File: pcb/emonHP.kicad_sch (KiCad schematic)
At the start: 23 parts, among them J1 USB_C_Receptacle_USB2.0, J2 Screw_Terminal_01x03, J3 Screw_Terminal_01x03, J4 Screw_Terminal_01x03, J5 Screw_Terminal_01x03, J6 Screw_Terminal_01x03, J7 Conn_ARM_JTAG_SWD_10, J8 Raspberry_Pi_2_3, U1 ATSAMD21G17A-A, U2 USBLC6-2P6, U3 AP2112K-3.3, U4 THVD1400D

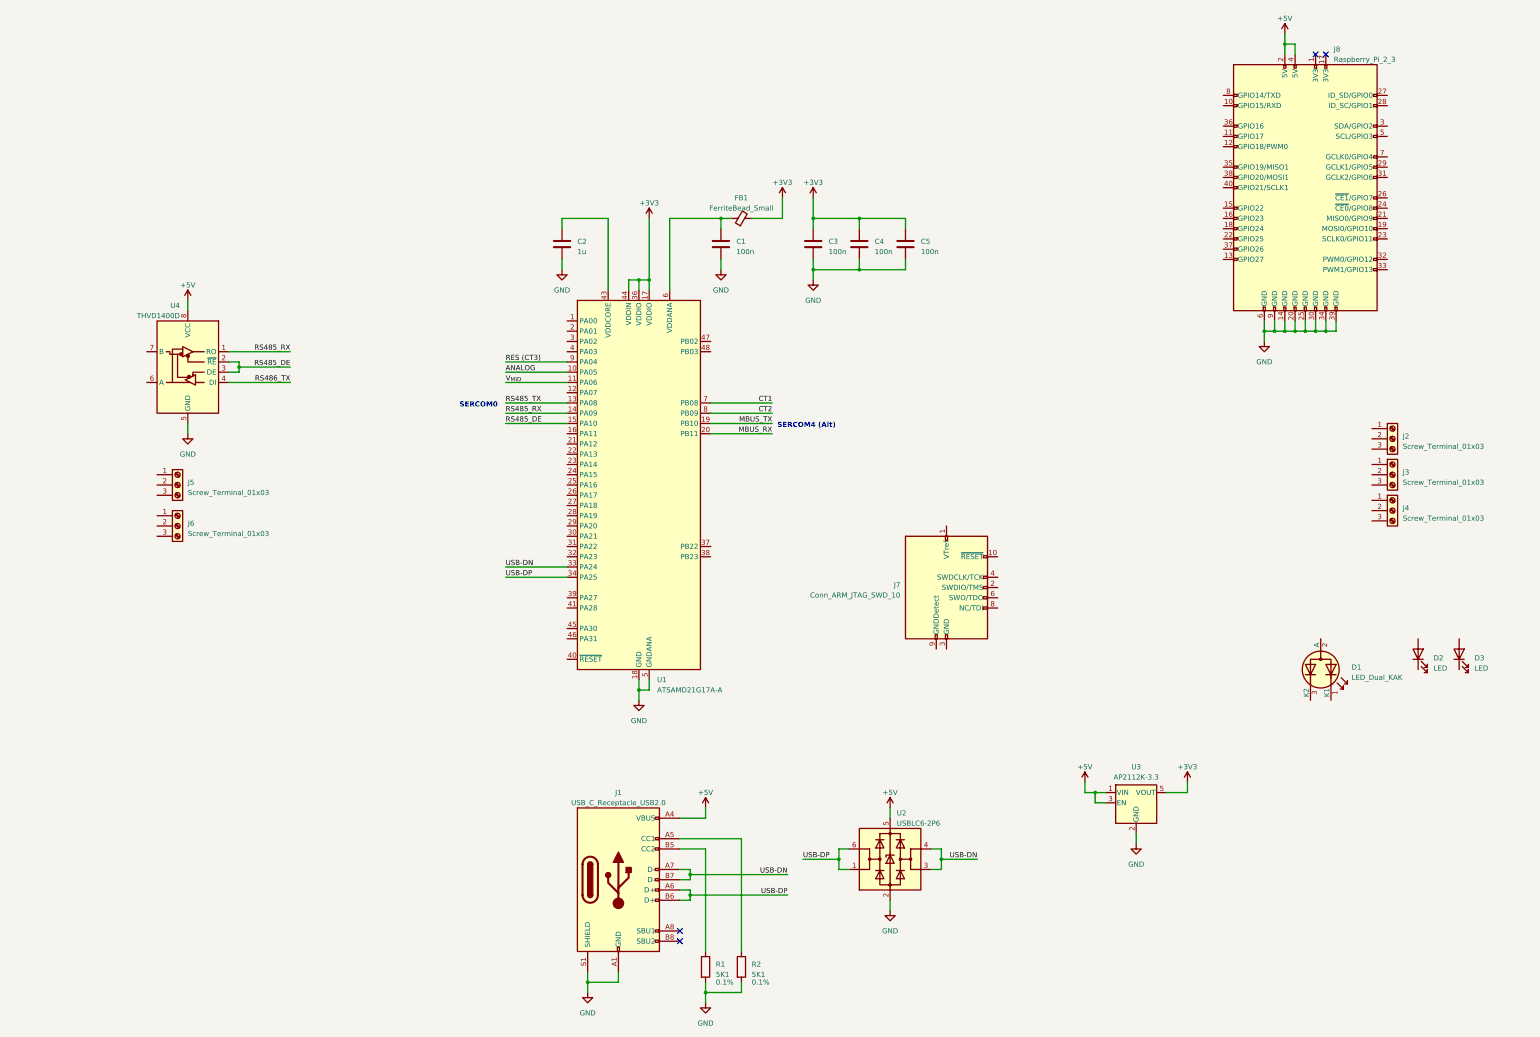
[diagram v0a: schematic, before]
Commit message: * Continue initial placement
  - External connectors added
  - Switch and indicator LED added
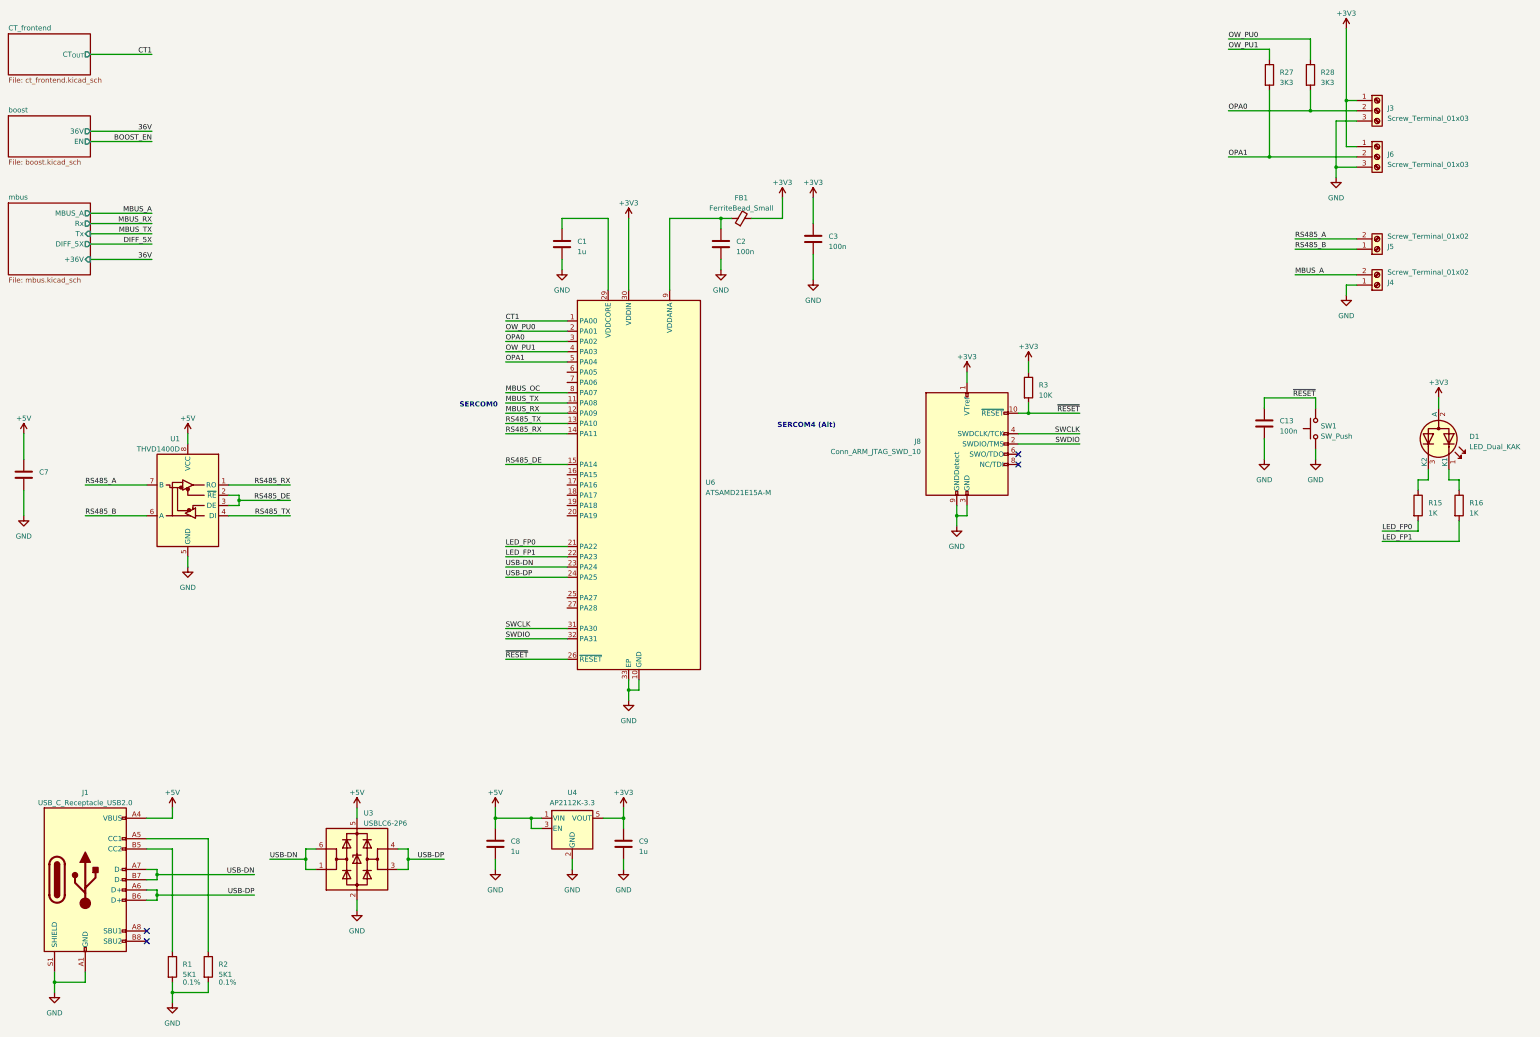
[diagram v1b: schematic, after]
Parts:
- removed C4, C5: 100n, Capacitor_SMD:C_0603_1608Metric, symbol Device:C
- removed D2, D3: LED, LED_SMD:LED_0805_2012Metric, symbol Device:LED
- removed J3, J4, J5: Screw_Terminal_01x03, TerminalBlock_Phoenix:TerminalBlock_Phoenix_PT-1,5-3-3.5-H_1x03_P3.50mm_Horizontal, symbol Connector:Screw_Terminal_01x03
- removed J7: Conn_ARM_JTAG_SWD_10, Connector_PinHeader_1.27mm:PinHeader_2x05_P1.27mm_Vertical_SMD, symbol Connector:Conn_ARM_JTAG_SWD_10
- removed J8: Raspberry_Pi_2_3, Connector_PinSocket_2.54mm:PinSocket_2x20_P2.54mm_Vertical_SMD, symbol Connector:Raspberry_Pi_2_3
- removed U1: ATSAMD21G17A-A, Package_QFP:TQFP-48_7x7mm_P0.5mm, symbol MCU_Microchip_SAMD:ATSAMD21G17A-A
- added C13, C7: 100n, Capacitor_SMD:C_0402_1005Metric, symbol Device:C
- added C8, C9: 1u, Capacitor_SMD:C_0402_1005Metric, symbol Device:C
- added J4, J5: Screw_Terminal_01x02, TerminalBlock_Phoenix:TerminalBlock_Phoenix_PT-1,5-2-3.5-H_1x02_P3.50mm_Horizontal, symbol Connector:Screw_Terminal_01x02
- added J8: Conn_ARM_JTAG_SWD_10, Connector_PinHeader_1.27mm:PinHeader_2x05_P1.27mm_Vertical_SMD, symbol Connector:Conn_ARM_JTAG_SWD_10
- added R15, R16: 1K, Resistor_SMD:R_0402_1005Metric, symbol Device:R
- added R27, R28: 3K3, Resistor_SMD:R_0402_1005Metric, symbol Device:R
- added R3: 10K, Resistor_SMD:R_0402_1005Metric, symbol Device:R
- added SW1: SW_Push, Button_Switch_SMD:Panasonic_EVQPUM_EVQPUD, symbol Switch:SW_Push
- added U6: ATSAMD21E15A-M, Package_DFN_QFN:QFN-32-1EP_5x5mm_P0.5mm_EP3.6x3.6mm, symbol MCU_Microchip_SAMD:ATSAMD21E15A-M
- C1: renamed from C2; footprint Capacitor_SMD:C_0603_1608Metric -> Capacitor_SMD:C_0402_1005Metric
- C2: renamed from C1; footprint Capacitor_SMD:C_0603_1608Metric -> Capacitor_SMD:C_0402_1005Metric
- C3: footprint Capacitor_SMD:C_0603_1608Metric -> Capacitor_SMD:C_0402_1005Metric
- FB1: footprint Inductor_SMD:L_0603_1608Metric -> Inductor_SMD:L_0402_1005Metric
- J1: footprint (none) -> valcon-usb:CSP-USC16-TR
- R1, R2: footprint (none) -> Resistor_SMD:R_0402_1005Metric
- renumbered J2 to J3, U4 to U1, U2 to U3, U3 to U4
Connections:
- net RS486_TX is gone; now on net RS485_TX: U1.4 (DI)
- net +3V3: now also D1.2 (A), J3.1 (Pin_1), J6.1 (Pin_1), C9.1, J8.1 (VTref), R3.1, U6.30 (VDDIN)
- net +5V: now also C7.1, C8.1
- net CT1: now also U6.1 (PA00)
- net GND: now also J3.3 (Pin_3), J6.3 (Pin_3), C13.2, C7.2, C8.2, C9.2, J4.1 (Pin_1), J8.3 (GND), J8.5 (GND), J8.9 (GNDDetect), SW1.1, U6.10 (GND), U6.28 (GND), U6.33 (EP)
- net MBUS_RX: now also U6.12 (PA09)
- net MBUS_TX: now also U6.11 (PA08)
- net RS485_DE: now also U6.15 (PA14)
- net RS485_RX: now also U6.14 (PA11)
- net RS485_TX: now also U6.13 (PA10)
- net USB-DN: now also U3.1 (I/O1), U3.6 (I/O1), U6.23 (PA24); no longer U3.3 (I/O2), U3.4 (I/O2)
- net USB-DP: now also U3.3 (I/O2), U3.4 (I/O2), U6.24 (PA25); no longer U3.1 (I/O1), U3.6 (I/O1)
- net OPA1: now reaches J6.2 (Pin_2)
- net OPA1: now also R27.2, U6.5 (PA04)
- net at C1.1: now also U6.29 (VDDCORE)
- net at C2.1, FB1.1: now also U6.9 (VDDANA)
- net OPA0: now reaches J3.2 (Pin_2)
- net OPA0: now also R28.2, U6.3 (PA02)
- net at D1.1 (K1): now also R16.1
- net at D1.3 (K2): now also R15.1
- net RS485_B: now reaches U1.6 (A)
- net RS485_B: now also J5.1 (Pin_1)
- net RS485_A: now reaches U1.7 (B)
- net RS485_A: now also J5.2 (Pin_2)
- new net LED_FP0: R15.2, U6.21 (PA22)
- new net LED_FP1: R16.2, U6.22 (PA23)
- new net MBUS_A: J4.2 (Pin_2)
- new net MBUS_OC: U6.8 (PA07)
- new net OW_PU0: R28.1, U6.2 (PA01)
- new net OW_PU1: R27.1, U6.4 (PA03)
- new net SWCLK: J8.4 (SWDCLK/TCK), U6.31 (PA30)
- new net SWDIO: J8.2 (SWDIO/TMS), U6.32 (PA31)
- new net ~{RESET}: C13.1, J8.10 (~{RESET}), R3.2, SW1.2, U6.26 (~{RESET})
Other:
- added sheet CT_frontend (ct_frontend.kicad_sch)
- added sheet boost (boost.kicad_sch)
- added sheet mbus (mbus.kicad_sch)
- company: OpenEnergyMonitor / Tilt Ltd -> Tilt Ltd / OpenEnergyMonitor
- moved on the sheet: C3, D1, J1, J3, R1, R2, U1, U3, U4

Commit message: * Work in progress
  - Add generate script
  - Add switch model
  - Start routing
  - Tidy schematic
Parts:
- added D10: LED, LED_SMD:LED_0805_2012Metric, symbol Device:LED
- added D13 (x3): ESD5Z3.3T5G, Diode_SMD:D_SOD-523, symbol Diode:ESD5Zxx
- added D5: CDSOT23-SM712, Package_TO_SOT_SMD:SOT-23, symbol Power_Protection:NUP2105L
- added J2: Conn_01x03, Connector_PinHeader_2.54mm:PinHeader_1x03_P2.54mm_Vertical, symbol Connector_Generic:Conn_01x03
- added R29, R30: 10R, Resistor_SMD:R_0603_1608Metric, symbol Device:R
- added R33: 1K, Resistor_SMD:R_0402_1005Metric, symbol Device:R
- J8: now not fitted
- SW1: footprint Button_Switch_SMD:Panasonic_EVQPUM_EVQPUD -> Button_Switch_SMD:Panasonic_EVQPUJ_EVQPUA
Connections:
- net +3V3: now also R33.1
- net BOOST_EN: now also U6.16 (PA15)
- net CT1: now also U6.3 (PA02); no longer U6.1 (PA00)
- net GND: now also D10.1 (K), D13.2 (A), D13.2 (A), D13.2 (A), D5.3 (A), J2.3 (Pin_3)
- net OPA0: now also U6.5 (PA04), D13.1 (K); no longer U6.3 (PA02)
- net OPA1: now also U6.7 (PA06), D13.1 (K); no longer U6.5 (PA04)
- net OW_PU0: now also U6.4 (PA03); no longer U6.2 (PA01)
- net OW_PU1: now also U6.6 (PA05); no longer U6.4 (PA03)
- net RS485_A: now also D5.1 (K), R29.1; no longer U1.7 (B)
- net RS485_B: now also D5.2 (K), R30.1; no longer U1.6 (A)
- net ~{RESET}: now also D13.1 (K)
- net DBG_TX: now reaches U6.19 (PA18)
- net DBG_TX: now also J2.1 (Pin_1)
- net DBG_RX: now reaches U6.20 (PA19)
- net DBG_RX: now also J2.2 (Pin_2)
- new net: D10.2 (A), R33.2
- new net: R29.2, U1.7 (B)
- new net: R30.2, U1.6 (A)
- no-connect marks 4 -> 10
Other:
- sheet mbus ports: added MBUS_OC; removed DIFF_5X
- note added: "AC (AIN[3])"
- note added: "ADC (AIN[0])"
- note added: "ADC (AIN[4])"
- note added: "ADC (AIN[6])"
- note added: "Microcontroller"
- note added: "RS485 with input protection"
- note added: "SERCOM1"
- note added: "SERCOM2 (ALT)"
- note added: "Terminal blocks"
- note added: "User indications"
- note removed: "SERCOM4 (Alt)"
- moved on the sheet: C1, C13, C2, C3, C7, C8, C9, D1, FB1, J4, J5, R15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

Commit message: * [0.1-dev] Voltage good
  - Add 36V voltage good detection
  - Add all 3D models
  - Correct footprint for front LED
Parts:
- removed J3, J6: Screw_Terminal_01x03, TerminalBlock_Phoenix:TerminalBlock_Phoenix_PT-1,5-3-3.5-H_1x03_P3.50mm_Horizontal, symbol Connector:Screw_Terminal_01x03
- added J9: Screw_Terminal_01x06, TerminalBlock_Phoenix:TerminalBlock_Phoenix_PT-1,5-6-3.5-H_1x06_P3.50mm_Horizontal, symbol Connector:Screw_Terminal_01x06
- added Q5: Q_NPN_BEC_BRT, Package_TO_SOT_SMD:SOT-23, symbol Device:Q_NPN_BEC_BRT
- added R35: 3K3, Resistor_SMD:R_0402_1005Metric, symbol Device:R
- D1: value LED_Dual_KAK -> LTST-S326KGJRKT; footprint LED_SMD:LED_LiteOn_LTST-S326 -> ltst-s326:LTST-S326; MPN (none) -> LTST-S326KGJRKT; Mouser (none) -> 859-LTST-S326KGJRKT
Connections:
- net +3V3: now also J9.1 (Pin_1), J9.4 (Pin_4); no longer D1.2 (A)
- net +5V: now also D1.2 (A)
- net BOOST_EN: now also U6.20 (PA19), R35.1; no longer U6.16 (PA15)
- net DBG_RX: now also U6.18 (PA17); no longer U6.20 (PA19)
- net DBG_TX: now also U6.17 (PA16); no longer U6.19 (PA18)
- net GND: now also J9.3 (Pin_3), J9.6 (Pin_6), Q5.2 (E)
- net OPA0: now also J9.2 (Pin_2)
- net OPA1: now also J9.5 (Pin_5)
- new net 36V_RG: U6.16 (PA15)
- new net BOOST_EN_PROT: Q5.3 (C), R35.2
- new net OC_CMP_OUT: Q5.1 (B), U6.19 (PA18)
- no-connect marks 10 -> 8
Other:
- sheet boost ports: added 36V_RG; removed none

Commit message: * [0.1-dev] Add git commit references and README
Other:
- note added: "Creative Commons Attribution-ShareAlike 4.0 License Design is provided AS IS and WITH ALL FAULTS. All other WARRANTIES, express or implied, are DISCLAIMED."
- moved on the sheet: C13, D1, D10, D13, J1, R1, R15, R16, R2, R33, SW1, U3

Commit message: * Swap reset button for cheap onboard
  - Can access bootloader from serial, no need for front panel
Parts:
- SW1: footprint Button_Switch_SMD:Panasonic_EVQPUJ_EVQPUA -> Button_Switch_SMD:SW_Tactile_SPST_NO_Straight_CK_PTS636Sx25SMTRLFS
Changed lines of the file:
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@@
       (effects (font (size 1.27 1.27)) (justify right))
     )
-    (property "Footprint" "Button_Switch_SMD:Panasonic_EVQPUJ_EVQPUA" (at 318.77 173.99 0)
+    (property "Footprint" "Button_Switch_SMD:SW_Tactile_SPST_NO_Straight_CK_PTS636Sx25SMTRLFS" (at 318.77 173.99 0)
       (effects (font (size 1.27 1.27)) hide)
     )

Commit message: [v0.1-dev] First pass on emonPi format
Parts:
- removed C1: 1u, Capacitor_SMD:C_0402_1005Metric, symbol Device:C
- removed C3: 100n, Capacitor_SMD:C_0402_1005Metric, symbol Device:C
- removed D1: LTST-S326KGJRKT, ltst-s326:LTST-S326, symbol Device:LED_Dual_KAK
- removed D10: LED, LED_SMD:LED_0805_2012Metric, symbol Device:LED
- removed D13 (x3): ESD5Z3.3T5G, Diode_SMD:D_SOD-523, symbol Diode:ESD5Zxx
- removed D5: CDSOT23-SM712, Package_TO_SOT_SMD:SOT-23, symbol Power_Protection:NUP2105L
- removed FB1: FerriteBead_Small, Inductor_SMD:L_0402_1005Metric, symbol Device:FerriteBead_Small
- removed J1: USB_C_Receptacle_USB2.0, valcon-usb:CSP-USC16-TR, symbol Connector:USB_C_Receptacle_USB2.0
- removed J2: Conn_01x03, Connector_PinHeader_2.54mm:PinHeader_1x03_P2.54mm_Vertical, symbol Connector_Generic:Conn_01x03
- removed J4, J5: Screw_Terminal_01x02, TerminalBlock_Phoenix:TerminalBlock_Phoenix_PT-1,5-2-3.5-H_1x02_P3.50mm_Horizontal, symbol Connector:Screw_Terminal_01x02
- removed J8: Conn_ARM_JTAG_SWD_10, Connector_PinHeader_1.27mm:PinHeader_2x05_P1.27mm_Vertical_SMD, symbol Connector:Conn_ARM_JTAG_SWD_10
- removed J9: Screw_Terminal_01x06, TerminalBlock_Phoenix:TerminalBlock_Phoenix_PT-1,5-6-3.5-H_1x06_P3.50mm_Horizontal, symbol Connector:Screw_Terminal_01x06
- removed Q5: Q_NPN_BEC_BRT, Package_TO_SOT_SMD:SOT-23, symbol Device:Q_NPN_BEC_BRT
- removed R15, R16, R33: 1K, Resistor_SMD:R_0402_1005Metric, symbol Device:R
- removed R2: 5K1, Resistor_SMD:R_0402_1005Metric, symbol Device:R
- removed R27, R28, R35: 3K3, Resistor_SMD:R_0402_1005Metric, symbol Device:R
- removed R29, R30: 10R, Resistor_SMD:R_0603_1608Metric, symbol Device:R
- removed U1: THVD1400D, Package_SO:SOIC-8_3.9x4.9mm_P1.27mm, symbol Interface_UART:THVD1400D
- removed U3: USBLC6-2P6, Package_TO_SOT_SMD:SOT-666, symbol Power_Protection:USBLC6-2P6
- removed U4: AP2112K-3.3, Package_TO_SOT_SMD:SOT-23-5, symbol Regulator_Linear:AP2112K-3.3
- removed U6: ATSAMD21E15A-M, Package_DFN_QFN:QFN-32-1EP_5x5mm_P0.5mm_EP3.6x3.6mm, symbol MCU_Microchip_SAMD:ATSAMD21E15A-M
- added C10, C11, C15, C6: 100n, Capacitor_SMD:C_0402_1005Metric, symbol Device:C
- added C12: 1u, Capacitor_SMD:C_0402_1005Metric, symbol Device:C
- added C14, C4, C5: 2u2, Capacitor_SMD:C_0603_1608Metric, symbol Device:C
- added CN1, CN4: CONN_03SCREW, TerminalBlock_Phoenix:TerminalBlock_Phoenix_PT-1,5-3-3.5-H_1x03_P3.50mm_Horizontal, symbol Connector:Screw_Terminal_01x03
- added CN3: Screw_Terminal_01x02, TerminalBlock_Phoenix:TerminalBlock_Phoenix_PT-1,5-2-3.5-H_1x02_P3.50mm_Horizontal, symbol Connector:Screw_Terminal_01x02
- added CN5: Screw_Terminal_01x02, TerminalBlock_Phoenix:TerminalBlock_Phoenix_PT-1,5-2-5.0-H_1x02_P5.00mm_Horizontal, symbol Connector:Screw_Terminal_01x02
- added D2, D3, D4: ESD5Z3.3T5G, Diode_SMD:D_SOD-523, symbol Diode:ESD5Zxx
- added FB1, FB2: FerriteBead, Resistor_SMD:R_0402_1005Metric, symbol Device:FerriteBead
- added FD1, FD2, FD3: FIDUCIAL1X2, Fiducial:Fiducial_0.75mm_Mask1.5mm, symbol Mechanical:Fiducial
- added H1, H2: MountingHole, MountingHole:MountingHole_2.7mm_M2.5, symbol Mechanical:MountingHole
- added H3: MountingHole, MountingHole:MountingHole_2.1mm, symbol Mechanical:MountingHole
- added J1, J2: CONN_04PTH, Connector_PinSocket_2.54mm:PinSocket_1x04_P2.54mm_Vertical, symbol Connector_Generic:Conn_01x04
- added J3: USB_C_Receptacle_USB2.0, valcon-usb:CSP-USC16-TR, symbol Connector:USB_C_Receptacle_USB2.0
- added J4: Conn_ARM_JTAG_SWD_10, Connector_PinHeader_1.27mm:PinHeader_2x05_P1.27mm_Vertical_SMD, symbol Connector:Conn_ARM_JTAG_SWD_10
- added J5: Conn_02x20_Odd_Even, RPi-SMD:REF-182665, symbol Connector_Generic:Conn_02x20_Odd_Even
- added JP1: Jumper_2_Open, Jumper:SolderJumper-2_P1.3mm_Open_TrianglePad1.0x1.5mm, symbol Jumper:Jumper_2_Open
- added LED1: LED_Dual_KAK, ltst-s326:LTST-S326, symbol Device:LED_Dual_KAK
- added R10, R6, R8, R9: 1K, Resistor_SMD:R_0402_1005Metric, symbol Device:R
- added R11, R7: 10K, Resistor_SMD:R_0402_1005Metric, symbol Device:R
- added R17: 47K, Resistor_SMD:R_0402_1005Metric, symbol Device:R
- added R18, R19: 4K7, Resistor_SMD:R_0402_1005Metric, symbol Device:R
- added R4, R5: 5K1, Resistor_SMD:R_0402_1005Metric, symbol Device:R
- added SMA1: SMACONNECTOR, Connector_Coaxial:SMA_Amphenol_132203-12_Horizontal, symbol Connector:Conn_Coaxial
- added SW2: SW_Push, Button_Switch_SMD:SW_Tactile_SPST_NO_Straight_CK_PTS636Sx25SMTRLFS, symbol Switch:SW_Push
- added TP1, TP4, TP5, TP6, TP7, TP8: TestPoint, TestPoint:TestPoint_Pad_D1.0mm, symbol Connector:TestPoint
- added U10: SN74LVC1T45DRL, Package_TO_SOT_SMD:SOT-563, symbol Logic_LevelTranslator:SN74LVC1T45DRL
- added U2: ATSAMD21G15B-A, Package_QFP:TQFP-48_7x7mm_P0.5mm, symbol MCU_Microchip_SAMD:ATSAMD21G15B-A
- added U3: AP2112K-3.3, Package_TO_SOT_SMD:SOT-23-5, symbol Regulator_Linear:AP2112K-3.3
- added U4: RFM69CW, rfm69cw:RFM69CW, symbol rfm69cw:RFM69CW
- added U9: USBLC6-2P6, Package_TO_SOT_SMD:SOT-666, symbol Power_Protection:USBLC6-2P6
- C13, C7: value 100n -> 2u2; footprint Capacitor_SMD:C_0402_1005Metric -> Capacitor_SMD:C_0603_1608Metric; Voltage (none) -> 6V
- C2: value 100n -> 2u2; footprint Capacitor_SMD:C_0402_1005Metric -> Capacitor_SMD:C_0603_1608Metric; Voltage (none) -> 16V
- C8, C9: value 1u -> 100n
- R1: value 5K1 -> 4K7; Tolerance 0.1% -> (none)
- R3: value 10K -> 1K
- SW1: footprint Button_Switch_SMD:SW_Tactile_SPST_NO_Straight_CK_PTS636Sx25SMTRLFS -> Button_Switch_THT:SW_PUSH_6mm; now not fitted
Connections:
- net +3V3: now also C7.1, R1.2, C14.1, C5.2, CN1.3 (Pin_3), FB1.1, FB2.1, J1.3 (Pin_3), J2.3 (Pin_3), LED1.2 (A), R17.2, R18.1, R19.1, R7.1, U10.1 (VCCA), U10.5 (DIR), U3.5 (VOUT); no longer C9.1, R3.1
- net +5V: now also C13.1, C2.2, C4.2, J3.A4 (VBUS), J3.A9 (VBUS), J3.B4 (VBUS), J3.B9 (VBUS), J5.2 (Pin_2), J5.4 (Pin_4), JP1.2 (B), TP1.1, U10.6 (VCCB), U3.1 (VIN), U3.3 (EN), U9.5 (VBUS); no longer C7.1, C8.1
- net GND: now also C2.1, C10.2, C11.2, C12.2, C14.2, C15.2, C4.1, C5.1, C6.2, CN1.1 (Pin_1), CN3.1 (Pin_1), CN4.3 (Pin_3), D2.2 (A), D3.2 (A), D4.2 (A), J1.4 (Pin_4), J2.4 (Pin_4), J3.A1 (GND), J3.A12 (GND), J3.B1 (GND), J3.B12 (GND), J3.S1 (SHIELD), J4.3 (GND), J4.5 (GND), J4.9 (GNDDetect), J5.14 (Pin_14), J5.20 (Pin_20), J5.30 (Pin_30), J5.34 (Pin_34), J5.39 (Pin_39), J5.6 (Pin_6), J5.9 (Pin_9), R4.1, R5.1, SMA1.2 (Ext), SW2.2, TP4.1, TP5.1, TP6.1, TP7.1, TP8.1, U10.2 (GND), U2.18 (GND), U2.35 (GND), U2.42 (GND), U2.5 (GNDANA), U3.2 (GND), U4.14 (GND), U4.3 (GND), U9.2 (GND); no longer C2.2, R1.2
- net OPA1: now also R1.1, CN1.2 (Pin_2), D2.1 (K), J5.37 (Pin_37), U2.1 (PA00)
- net SWCLK: now also J4.4 (SWDCLK/TCK), U2.45 (PA30)
- net SWDIO: now also J4.2 (SWDIO/TMS), U2.46 (PA31)
- net ~{RESET}: now also C6.1, J4.10 (~{RESET}), R10.2, R11.2, U2.40 (~{RESET}); no longer C13.1, R3.2, SW1.2
- new net: LED1.1 (K1), R9.2
- new net: LED1.3 (K2), R8.2
- new net: D4.1 (K), R10.1, SW2.1
- new net: R3.1, U2.12 (PA07)
- new net: C12.1, U2.43 (VDDCORE)
- new net: D3.1 (K), R6.1, R7.2, SW1.2
- new net: C15.1, FB2.2, U4.2 (VDD)
- new net: SMA1.1 (In), U4.1 (ANA)
- new net: J3.B5 (CC2), R4.2
- new net: J3.A5 (CC1), R5.2
- new net ACDetect/AC0: CN5.1 (Pin_1)
- new net ACDetect/AC1: CN5.2 (Pin_2)
- new net DHW_SENSE: J5.36 (Pin_36), U2.2 (PA01)
- new net I2C_SCL: J1.2 (Pin_2), J2.2 (Pin_2), J5.5 (Pin_5), R19.2, U2.26 (PA17)
- new net I2C_SDA: J1.1 (Pin_1), J2.1 (Pin_1), J5.3 (Pin_3), R18.2, U2.25 (PA16)
- new net MBUS_EN: JP1.1 (A)
- new net MBus/MBUS_A: CN3.2 (Pin_2)
- new net PI_3V3: J5.17 (Pin_17), R3.2
- new net RFM_IRQ: J5.22 (Pin_22), U4.9 (DIO0)
- new net RFM_MISO: J5.21 (Pin_21), U2.13 (PA08), U4.8 (MISO)
- new net RFM_MOSI: J5.19 (Pin_19), U2.16 (PA11), U4.5 (MOSI)
- new net RFM_RESET: J5.24 (Pin_24), U4.13 (RESET)
- new net RFM_SCK: J5.23 (Pin_23), U2.14 (PA09), U4.6 (SCK)
- new net RFM_SEL: J5.16 (Pin_16), R17.1, U2.15 (PA10), U4.7 (~{SS})
- new net RS485/RS485_A: CN4.1 (Pin_1)
- new net RS485/RS485_B: CN4.2 (Pin_2)
- new net RS485_RX5: U10.4 (B)
- new net UART0_RX: J5.8 (Pin_8), U2.21 (PA12)
- new net UART0_TX: J5.10 (Pin_10), U2.22 (PA13)
- new net UART3_RTS: J5.26 (Pin_26), J5.31 (Pin_31), U2.37 (PB22), U2.38 (PB23)
- new net UART3_RX: J5.29 (Pin_29), U10.3 (A), U2.32 (PA23)
- new net UART3_TX: J5.7 (Pin_7), U2.31 (PA22)
- new net UART5_RX: J5.33 (Pin_33), U2.29 (PA20)
- new net UART5_TX: J5.32 (Pin_32), U2.30 (PA21)
- new net USB_D+: J3.A6 (D+), J3.B6 (D+), U2.34 (PA25), U9.3 (I/O2), U9.4 (I/O2)
- new net USB_D-: J3.A7 (D-), J3.B7 (D-), U2.33 (PA24), U9.1 (I/O1), U9.6 (I/O1)
- new net Vuc: C10.1, C11.1, C8.1, C9.1, FB1.2, J4.1 (VTref), R11.1, U2.17 (VDDIO), U2.36 (VDDIO), U2.44 (VDDIN), U2.6 (VDDANA)
- new net ~{LCD_BUTTON}: J5.11 (Pin_11), R6.2
- new net ~{LED_PROG}: R9.1
- new net ~{LED_STATUS}: R8.1
- no-connect marks 8 -> 18
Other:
- removed sheet CT_frontend
- removed sheet boost
- removed sheet mbus
- added sheet ACDetect (ACDetect.kicad_sch)
- added sheet Boost (boost.kicad_sch)
- added sheet MBus (mbus.kicad_sch)
- added sheet RS485 (RS485.kicad_sch)
- note added: "Additional Current Sensors"
- note added: "CT Current Sensors"
- note added: "CTS ->"
- note added: "EEPROM"
- note added: "Fabrication"
- note added: "Hardware design files are licensed under the Creative Commons Attribution-ShareAlike 4.0 License Design is provided "AS IS" and "WITH ALL FAULTS. ALL OTHER WARRANTIES, EXPRESS OR IMPLIED, ARE DISCLAIMED."
- note added: "INT I2C"
- note added: "OLED"
- note added: "Optional Headers"
- note added: "Power Supply and Protection"
- note added: "Raspberry Pi Header"
- note added: "Temperature, Pulse, and Analog Inputs"
- note added: "USB and Protection"
- note added: "User Interface"
- note added: "Wireless Transmitter"
- note removed: "AC (AIN[3])"
- note removed: "ADC (AIN[0])"
- note removed: "ADC (AIN[4])"
- note removed: "ADC (AIN[6])"
- note removed: "Creative Commons Attribution-ShareAlike 4.0 License Design is provided AS IS and WITH ALL FAULTS. All other WARRANTIES, express or implied, are DISCLAIMED."
- note removed: "RS485 with input protection"
- note removed: "SERCOM0"
- note removed: "SERCOM1"
- note removed: "SERCOM2 (ALT)"
- note removed: "Terminal blocks"
- note removed: "User indications"
- company: Tilt Ltd / OpenEnergyMonitor -> OpenEnergyMonitor / Tilt Ltd (Angus Logan)
